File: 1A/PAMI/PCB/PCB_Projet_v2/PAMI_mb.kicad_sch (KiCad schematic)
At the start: 71 parts, among them J1 Conn_02x20_Odd_Even, J10 Conn_01x04, J11 Conn_01x04, J12 Conn_01x04, J13 Conn_01x04, J2 Conn_01x03, J3 Conn_ST_STDC14, J4 Battery, J5 Charge, J6 Stop, J8 173010542, J9 Conn_01x04, SW1 SW_Push_SPDT, SW2 RotaryEncoder_Switch, SW3 SW_Push, U1 STM32G431KBTx, U2 LT1076CR-PBF, U3 AZ1117CH2-3.3TRG1

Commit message: update pcb
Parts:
- L1: footprint Inductor_SMD:L_0201_0603Metric -> (none)
- SW1: footprint MINI_SPDT_SW:SW_MINI-SPDT-SW -> Library:472121010111; MPN (none) -> 472121010111
- SW3: footprint Button_Switch_THT:SW_PUSH_6mm -> Button_Switch_SMD:SW_Push_1P1T_NO_6x6mm_H9.5mm
- U3: footprint AZ1117_CH2:SOT230P700X180-4N -> Package_TO_SOT_SMD:SOT-223-3_TabPin2
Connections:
- net GND: now also J4.2 (Pin_2), J5.2 (Pin_2); no longer J4.1 (Pin_1), J5.1 (Pin_1)
- net PWM_MOTOR_L_TIM2_CH1: now also U1.11 (PA6); no longer U1.10 (PA5)
- net PWM_MOTOR_R_TIM3_CH1: now also U1.10 (PA5); no longer U1.11 (PA6)
- net TMC2225/OA1: now also J11.2 (Pin_2); no longer J11.1 (Pin_1)
- net TMC2225/OA2: now also J11.1 (Pin_1); no longer J11.2 (Pin_2)
- net TMC2226/OA1: now also J12.2 (Pin_2); no longer J12.1 (Pin_1)
- net TMC2226/OA2: now also J12.1 (Pin_1); no longer J12.2 (Pin_2)
- net VCC: now also J6.1 (Pin_1); no longer J6.2 (Pin_2)
- net V_BAT: now also J4.1 (Pin_1); no longer J4.2 (Pin_2)
- net V_CHARGE: now also J5.1 (Pin_1); no longer J5.2 (Pin_2)
- net at SW1.1 (A): now also J6.2 (Pin_2); no longer J6.1 (Pin_1)
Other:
- moved on the sheet: J4, J5, J6

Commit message: update PCB placement
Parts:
- C17, C18: footprint Capacitor_SMD:CP_Elec_6.3x5.4 -> Capacitor_SMD:CP_Elec_4x5.4
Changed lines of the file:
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@@
 			)
 		)
-		(property "Footprint" "Capacitor_SMD:CP_Elec_6.3x5.4"
+		(property "Footprint" "Capacitor_SMD:CP_Elec_4x5.4"
 			(at 256.54 86.36 0)
 			(effects
@@
 			)
 		)
-		(property "Footprint" "Capacitor_SMD:CP_Elec_6.3x5.4"
+		(property "Footprint" "Capacitor_SMD:CP_Elec_4x5.4"
 			(at 241.3 86.36 0)
 			(effects

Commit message: update PAMI pcb
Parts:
- removed C10, C6: 10n, Capacitor_SMD:C_0402_1005Metric, symbol Device:C_Small
- removed C17, C18: 10u, Capacitor_SMD:CP_Elec_4x5.4, symbol Device:C_Polarized_Small
- removed C8: 10u, Capacitor_SMD:C_0402_1005Metric, symbol Device:C_Polarized_Small
- added C106, C110: 10n, Capacitor_SMD:C_0402_1005Metric, symbol Device:C_Small
- added C117, C118: 10u, Capacitor_SMD:C_0603_1608Metric, symbol Device:C_Small
- L101: renamed from L1; footprint (none) -> Inductor_SMD:L_Wuerth_WE-PD2-Typ-L
- renumbered C1 to C101, C2 to C102, C3 to C103, C4 to C104, C5 to C105, C7 to C107, C9 to C109, C11 to C111, C12 to C112, C13 to C113, C14 to C114, C15 to C115, C16 to C116, CR1 to CR101, D1 to D101, D2 to D102, D3 to D103, D4 to D104, D5 to D105, D6 to D106, D7 to D107, D8 to D108, H1 to H101, H2 to H102, H3 to H103, H4 to H104, J1 to J101, J2 to J102, J3 to J103, J4 to J104, J5 to J105, J6 to J106, J13 to J107, J8 to J108, J9 to J109, J10 to J110, J11 to J111, J12 to J112, R1 to R101, R2 to R102, R5 to R103, R3 to R104, R4 to R105, R6 to R106, R7 to R107, R8 to R108, R9 to R109, R10 to R110, R11 to R111, R13 to R112, R14 to R113, R12 to R114, R15 to R115, R16 to R116, R17 to R117, R18 to R118, R19 to R119, R20 to R120, SW1 to SW101, SW2 to SW102, SW3 to SW103, TP1 to TP101, U1 to U101, U2 to U102, U3 to U103
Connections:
- net +3.3V: now also C118.1
- net +5V: now also C117.1
- net ENCODEUR_B: no longer C105.1
- net GND: now also SW102.S1, C106.2, C110.2, C117.2, C118.2; no longer SW102.S2
- net at R103.2, R107.1, SW102.B: now also C105.1
- net at R105.2, R109.1, SW102.A: now also C106.1
- net at R111.2, R114.1: now also SW102.S2, C110.1; no longer SW102.S1
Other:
- moved on the sheet: R103, R105, R114

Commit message: update pcb PAMI
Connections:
- net DIR_MOTOR_L: now also U101.12 (PA7); no longer U101.9 (PA4)
- net DIR_MOTOR_R: now also U101.9 (PA4); no longer U101.12 (PA7)
- net LIDAR_LP_RX: now also U101.20 (PA10); no longer U101.8 (PA3)
- net LIDAR_LP_TX: now also U101.29 (PB6); no longer U101.7 (PA2)
- net PA12_USR_BTN_2: now also U101.6 (PA1); no longer U101.22 (PA12)
- net PA1_USR_BTN_0: now also U101.22 (PA12); no longer U101.6 (PA1)
- net RASPBERRY_PI_RX: now also U101.8 (PA3); no longer U101.20 (PA10)
- net RASPBERRY_PI_TX: now also U101.7 (PA2); no longer U101.29 (PB6)
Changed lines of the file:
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@@
-		)
-	)
-	(label "DIR_MOTOR_L"
-		(at 85.09 41.91 180)
-		(fields_autoplaced yes)
-		(effects
-			(font
-				(size 1.27 1.27)
-			)
-			(justify right bottom)
 		)
 	)
@@
 		)
 	)
+	(label "RASPBERRY_PI_TX"
+		(at 85.09 36.83 180)
+		(fields_autoplaced yes)
+		(effects
+			(font
+				(size 1.27 1.27)
+			)
+			(justify right bottom)
+		)
+	)
 	(label "STLINK_TX"
 		(at 15.24 46.99 0)
@@
 		)
 	)
+	(label "PA12_USR_BTN_2"
+		(at 85.09 34.29 180)
+		(fields_autoplaced yes)
+		(effects
+			(font
+				(size 1.27 1.27)
+			)
+			(justify right bottom)
+		)
+	)
 	(label "LIDAR_LP_RX"
 		(at 182.88 154.94 0)
@@
 		)
 	)
-	(label "PA12_USR_BTN_2"
-		(at 85.09 62.23 180)
-		(fields_autoplaced yes)
-		(effects
-			(font
-				(size 1.27 1.27)
-			)
-			(justify right bottom)
-		)
-	)
 	(label "V_CHARGE"
 		(at 77.47 127 0)
@@
 		)
 	)
+	(label "DIR_MOTOR_L"
+		(at 85.09 49.53 180)
+		(fields_autoplaced yes)
+		(effects
+			(font
+				(size 1.27 1.27)
+			)
+			(justify right bottom)
+		)
+	)
 	(label "PWM_MOTOR_R_TIM3_CH1"
 		(at 85.09 44.45 180)
@@
 		)
 	)
-	(label "RASPBERRY_PI_TX"
-		(at 15.24 54.61 0)
-		(fields_autoplaced yes)
-		(effects
-			(font
-				(size 1.27 1.27)
-			)
-			(justify left bottom)
+	(label "DIR_MOTOR_R"
+		(at 85.09 41.91 180)
+		(fields_autoplaced yes)
+		(effects
+			(font
+				(size 1.27 1.27)
+			)
+			(justify right bottom)
 		)
 	)
@@
 		)
 	)
+	(label "LIDAR_LP_RX"
+		(at 85.09 57.15 180)
+		(fields_autoplaced yes)
+		(effects
+			(font
+				(size 1.27 1.27)
+			)
+			(justify right bottom)
+		)
+	)
 	(label "I2C_SDA"
 		(at 15.24 57.15 0)
@@
 		)
 	)
+	(label "PA1_USR_BTN_0"
+		(at 85.09 62.23 180)
+		(fields_autoplaced yes)
+		(effects
+			(font
+				(size 1.27 1.27)
+			)
+			(justify right bottom)
+		)
+	)
 	(label "I2C_SDA"
 		(at 187.96 137.16 0)
@@
 		)
 	)
-	(label "LIDAR_LP_TX"
-		(at 85.09 36.83 180)
-		(fields_autoplaced yes)
-		(effects
-			(font
-				(size 1.27 1.27)
-			)
-			(justify right bottom)
-		)
-	)
 	(label "PA11_USR_BTN_1"
 		(at 85.09 59.69 180)
@@
 		)
 	)
-	(label "PA1_USR_BTN_0"
-		(at 85.09 34.29 180)
-		(fields_autoplaced yes)
-		(effects
-			(font
-				(size 1.27 1.27)
-			)
-			(justify right bottom)
-		)
-	)
 	(label "DATA_RECEIVER"
 		(at 16.51 190.5 0)
@@
 		)
 	)
+	(label "RASPBERRY_PI_RX"
+		(at 85.09 39.37 180)
+		(fields_autoplaced yes)
+		(effects
+			(font
+				(size 1.27 1.27)
+			)
+			(justify right bottom)
+		)
+	)
 	(label "ENCODEUR_BTN"
 		(at 173.99 179.07 180)
@@
 		)
 	)
-	(label "DIR_MOTOR_R"
-		(at 85.09 49.53 180)
-		(fields_autoplaced yes)
-		(effects
-			(font
-				(size 1.27 1.27)
-			)
-			(justify right bottom)
-		)
-	)
 	(label "SWCLK"
 		(at 85.09 67.31 180)
@@
 		)
 	)
-	(label "LIDAR_LP_RX"
-		(at 85.09 39.37 180)
-		(fields_autoplaced yes)
-		(effects
-			(font
-				(size 1.27 1.27)
-			)
-			(justify right bottom)
-		)
-	)
 	(label "PB8-BOOT0_LED0"
 		(at 95.25 66.04 270)
@@
 		)
 	)
-	(label "RASPBERRY_PI_RX"
-		(at 85.09 57.15 180)
-		(fields_autoplaced yes)
-		(effects
-			(font
-				(size 1.27 1.27)
-			)
-			(justify right bottom)
-		)
-	)
 	(label "STLINK_TX"
 		(at 121.92 57.15 180)
@@
 		(fields_autoplaced yes)
 		(effects
+			(font
+				(size 1.27 1.27)
+			)
+			(justify left bottom)
+		)
+	)
+	(label "LIDAR_LP_TX"
+		(at 15.24 54.61 0)
+		(fields_autoplaced yes)
+		(effects

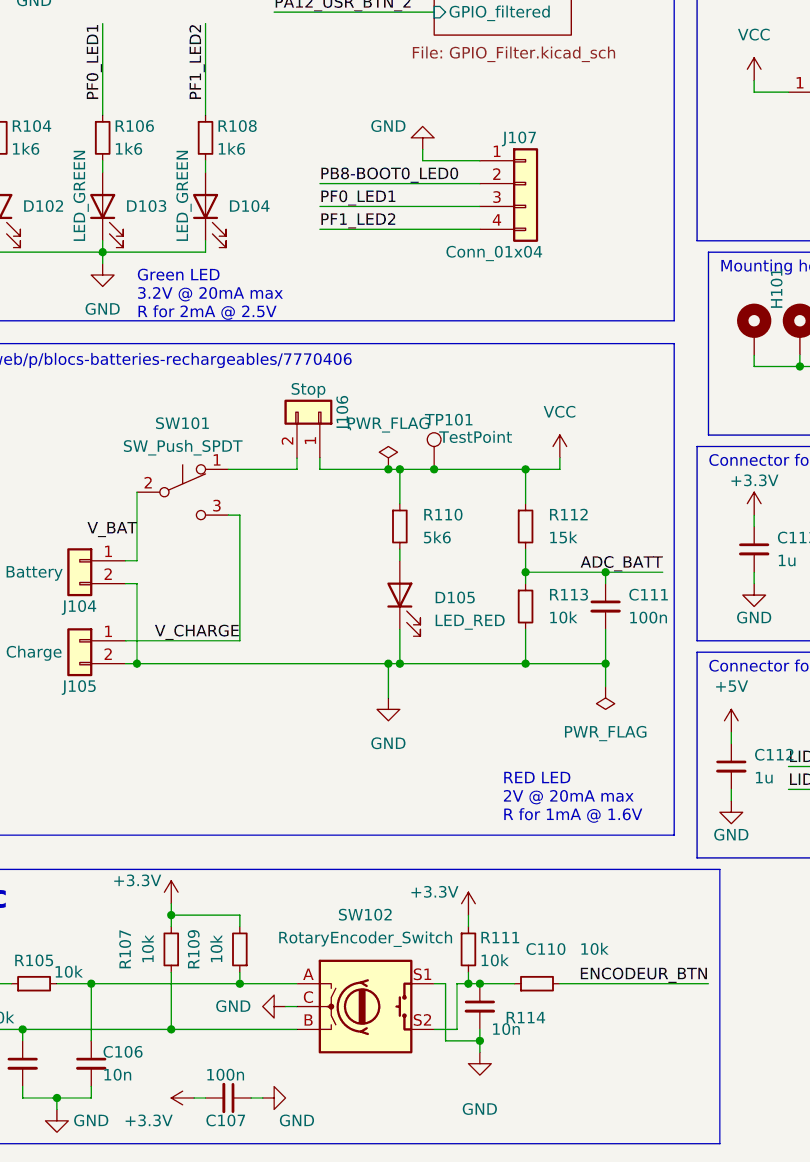
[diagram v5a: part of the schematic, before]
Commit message: pcb PAMI fix bugs
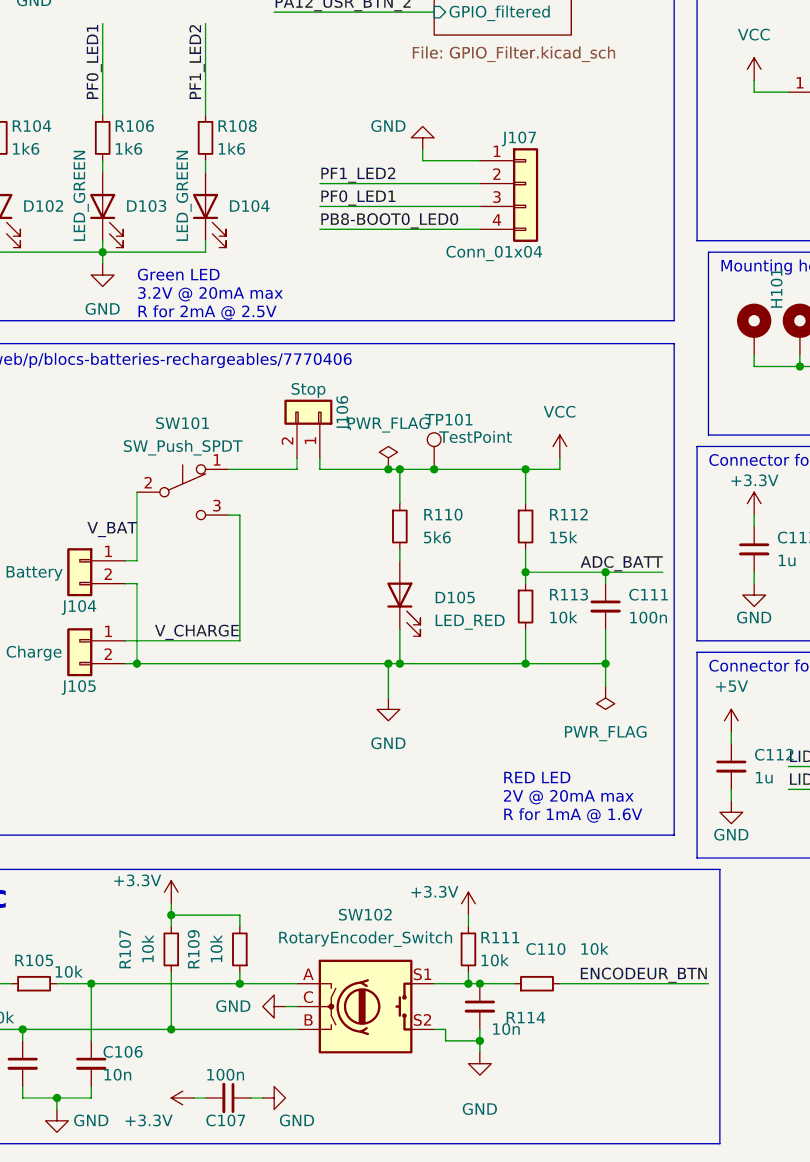
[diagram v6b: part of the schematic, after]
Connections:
- net GND: now also SW102.S2; no longer SW102.S1
- net PB8-BOOT0_LED0: now also J107.4 (Pin_4); no longer J107.2 (Pin_2)
- net PF1_LED2: now also J107.2 (Pin_2); no longer J107.4 (Pin_4)
- net at C110.1, R111.2, R114.1: now also SW102.S1; no longer SW102.S2
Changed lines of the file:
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@@
 	(wire
 		(pts
-			(xy 143.51 184.15) (xy 146.05 184.15)
-		)
-		(stroke
-			(width 0)
-			(type default)
-		)
-	)
-	(wire
-		(pts
 			(xy 147.32 179.07) (xy 148.59 179.07)
 		)
@@
 	(wire
 		(pts
-			(xy 146.05 179.07) (xy 146.05 184.15)
-		)
-		(stroke
-			(width 0)
-			(type default)
-		)
-	)
-	(wire
-		(pts
 			(xy 256.54 82.55) (xy 256.54 83.82)
 		)
@@
 	(wire
 		(pts
-			(xy 144.78 179.07) (xy 144.78 185.42)
-		)
-		(stroke
-			(width 0)
-			(type default)
-		)
-	)
-	(wire
-		(pts
 			(xy 191.77 160.02) (xy 194.31 160.02)
 		)
@@
 	(wire
 		(pts
-			(xy 143.51 179.07) (xy 144.78 179.07)
-		)
-		(stroke
-			(width 0)
-			(type default)
-		)
-	)
-	(wire
-		(pts
 			(xy 215.9 45.72) (xy 215.9 46.99)
 		)
@@
 	(wire
 		(pts
+			(xy 143.51 184.15) (xy 144.78 184.15)
+		)
+		(stroke
+			(width 0)
+			(type default)
+		)
+	)
+	(wire
+		(pts
 			(xy 232.41 36.83) (xy 234.95 36.83)
 		)
@@
 	(wire
 		(pts
-			(xy 147.32 179.07) (xy 146.05 179.07)
+			(xy 143.51 179.07) (xy 147.32 179.07)
 		)
 		(stroke
@@
 	(wire
 		(pts
+			(xy 144.78 185.42) (xy 144.78 184.15)
+		)
+		(stroke
+			(width 0)
+			(type default)
+		)
+	)
+	(wire
+		(pts
 			(xy 219.71 129.54) (xy 245.11 129.54)
 		)
@@
 		)
 	)
+	(label "PF1_LED2"
+		(at 130.81 90.17 0)
+		(fields_autoplaced yes)
+		(effects
+			(font
+				(size 1.27 1.27)
+			)
+			(justify left bottom)
+		)
+	)
+	(label "PB8-BOOT0_LED0"
+		(at 130.81 95.25 0)
+		(fields_autoplaced yes)
+		(effects
+			(font
+				(size 1.27 1.27)
+			)
+			(justify left bottom)
+		)
+	)
 	(label "NRST"
 		(at 121.92 31.75 180)
@@
 		)
 	)
-	(label "PB8-BOOT0_LED0"
-		(at 130.81 90.17 0)
-		(fields_autoplaced yes)
-		(effects
-			(font
-				(size 1.27 1.27)
-			)
-			(justify left bottom)
-		)
-	)
 	(label "PA11_USR_BTN_1"
 		(at 125.73 55.88 0)
@@
 		)
 	)
-	(label "PF1_LED2"
-		(at 130.81 95.25 0)
-		(fields_autoplaced yes)
-		(effects
-			(font
-				(size 1.27 1.27)
-			)
-			(justify left bottom)
-		)
-	)
